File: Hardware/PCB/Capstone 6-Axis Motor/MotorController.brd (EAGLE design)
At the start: 60.3 x 40.3 mm, 62 parts, among them CON3 TI-JTAG-CTI-20, J1 768250004CON_768250004_MOL, J2 768250004CON_768250004_MOL, J3 MF-CON-2.54mm-01x03, J4 MF-CON-2.54mm-01x03, J5 MF-CON-2.54mm-01x03, J6 MF-CON-2.54mm-01x03, J7 MF-CON-2.54mm-01x03, Q2 20MHz, U1 DRV8434SPWPR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

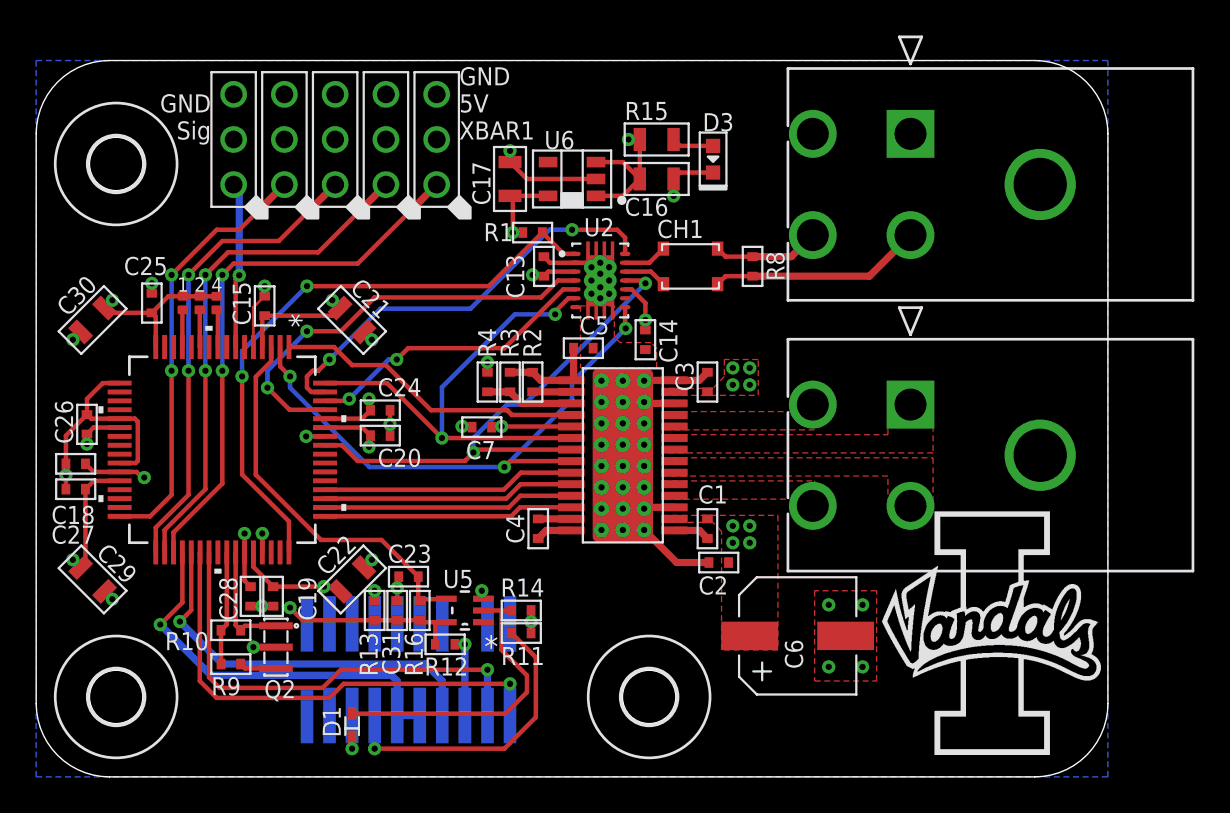
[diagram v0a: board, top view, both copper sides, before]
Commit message: Updated PCBs and added custom libraries
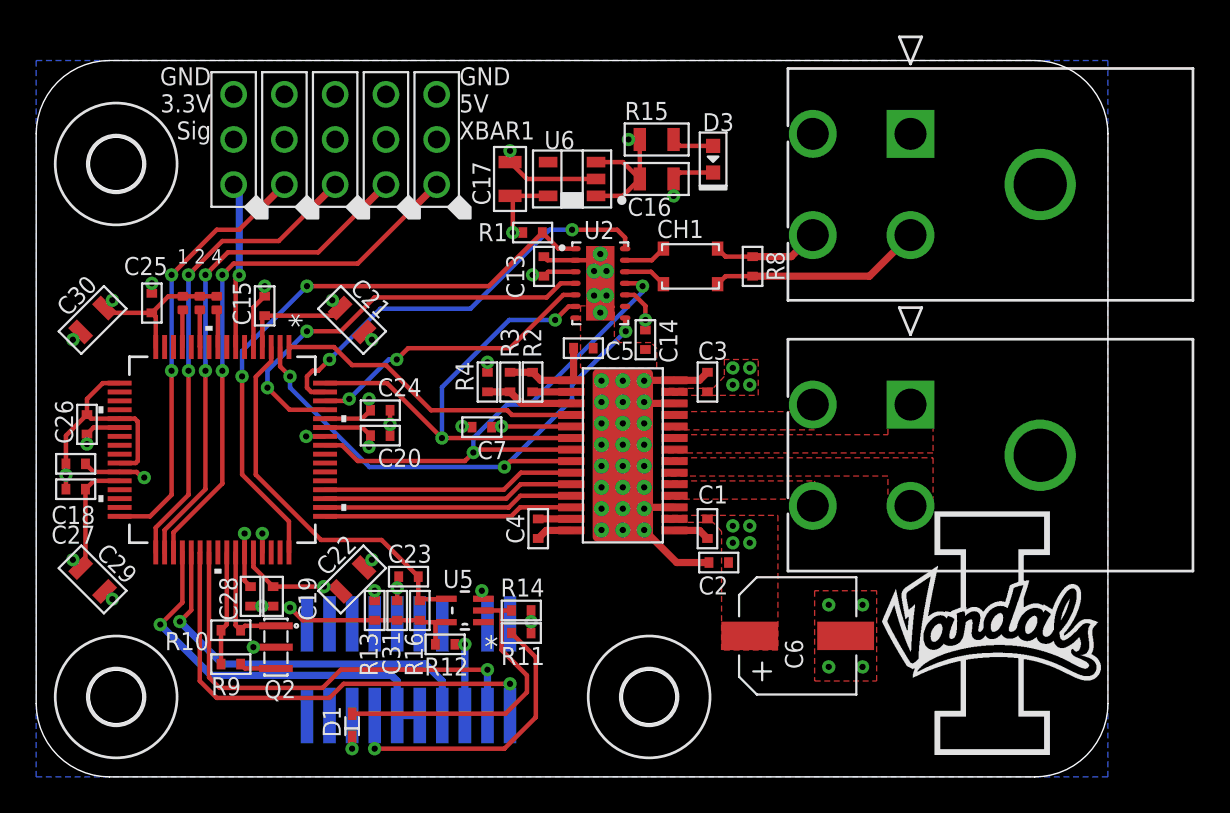
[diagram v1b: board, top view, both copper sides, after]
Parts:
- moved U2 0.16 mm to (31.8, 27.8)
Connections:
- net GND: no longer U2.15_10, U2.15_11, U2.15_12, U2.15_15, U2.15_16, U2.15_17, U2.15_21, U2.15_22, U2.15_23, U2.15_7, U2.15_8, U2.15_9
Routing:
- net GND: track 60.8 -> 54.8 mm
- net MCU_SCLK: track 32.2 -> 31.6 mm
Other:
- board text added: "GND 3.3V Sig"
- board text removed: "GND Sig"
